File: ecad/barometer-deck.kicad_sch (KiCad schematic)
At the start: 3 parts, among them P1 CF_EXP_LEFT, P2 CF_EXP_RIGHT

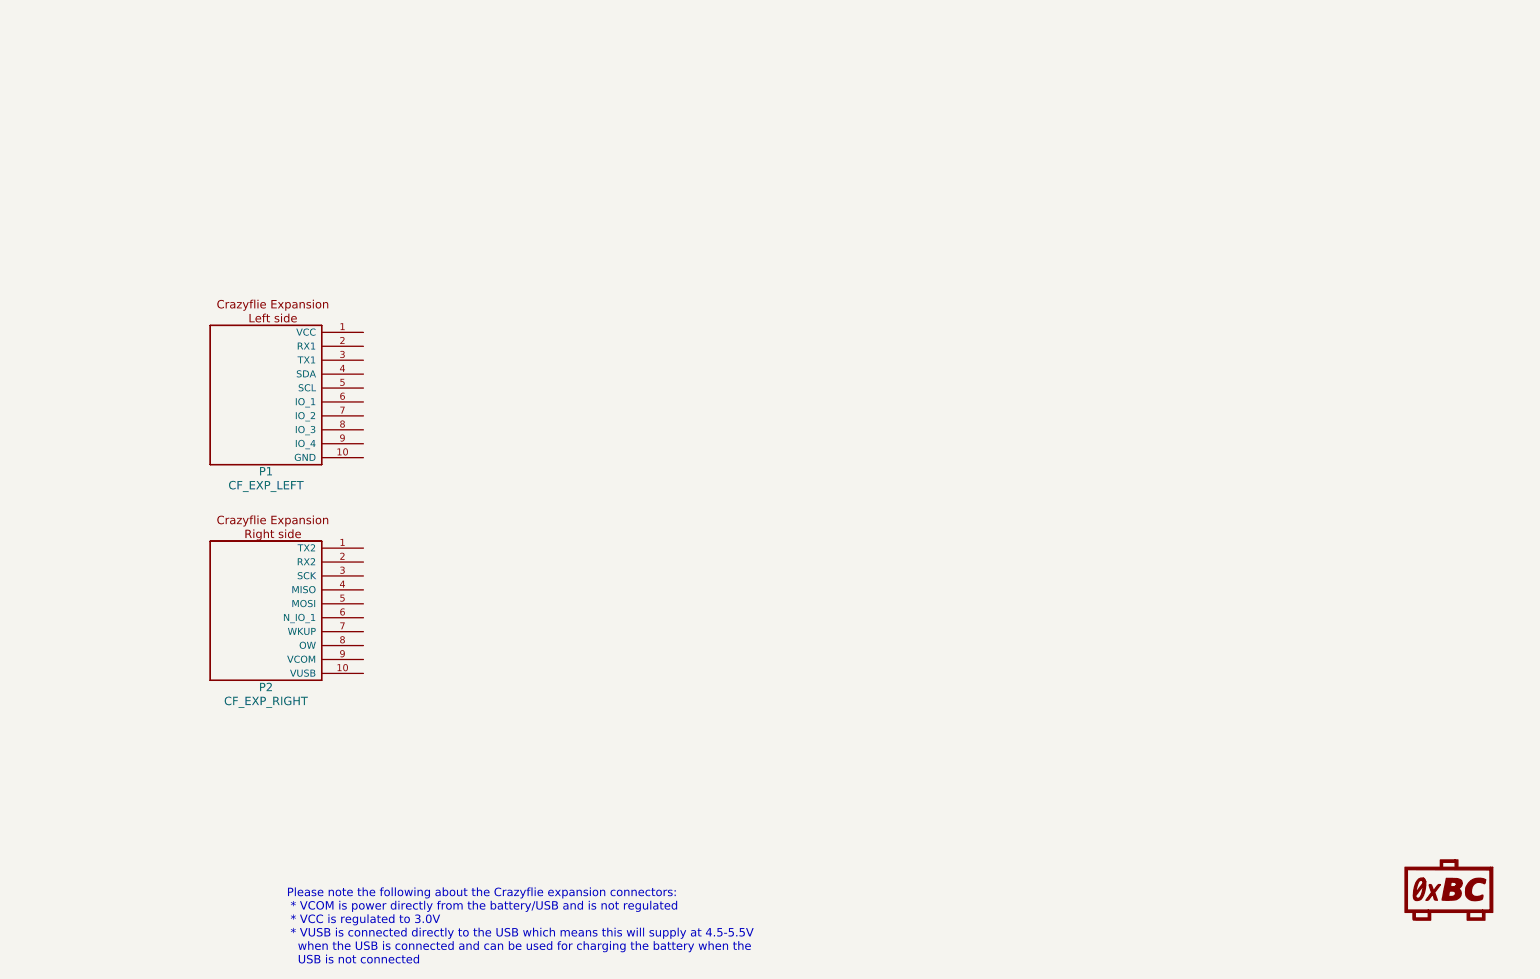
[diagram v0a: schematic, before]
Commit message: Initial schematics, power delviery module
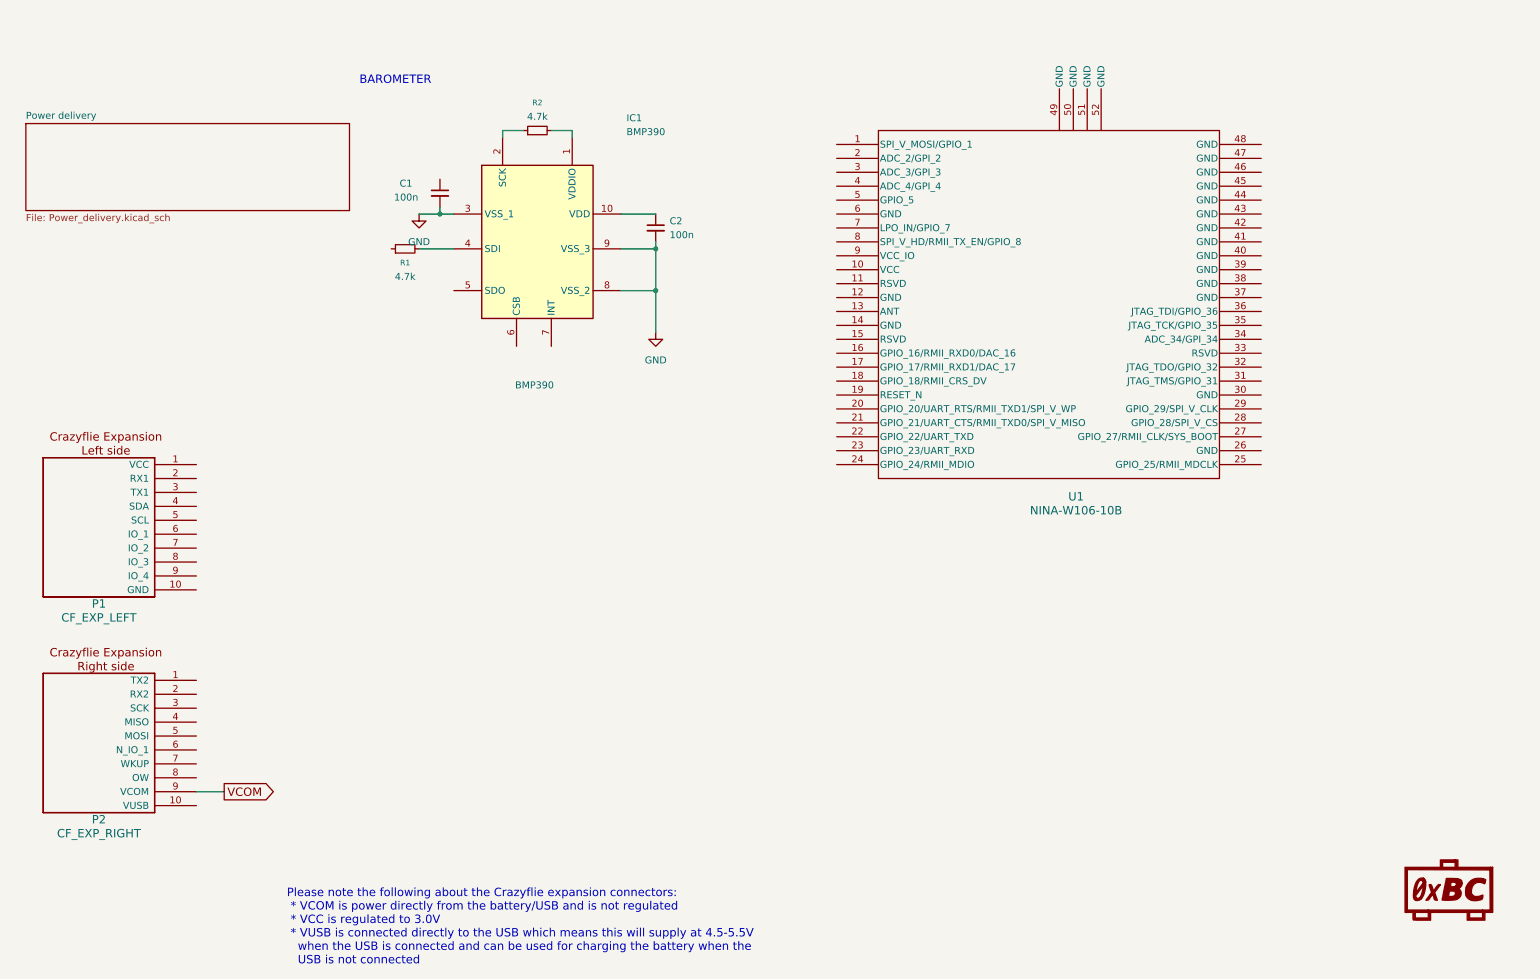
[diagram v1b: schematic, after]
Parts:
- added C1, C2: 100n, symbol PutRocketLab_RCL:C_Small
- added IC1: BMP390, BMP390, symbol BMP390:BMP390
- added R1, R2: 4.7k, symbol Device:R_Small
- added U1: NINA-W106-10B, NINA-W106_UBL, symbol NINA-W106_UBL:NINA-W106-10B
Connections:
- net VCOM: now reaches P2.9 (VCOM)
- new net: IC1.4 (SDI), R1.2
- new net: C2.1, IC1.10 (VDD)
- new net: IC1.2 (SCK), R2.1
- new net: IC1.1 (VDDIO), R2.2
- new net GND: C1.2, C2.2, IC1.3 (VSS_1), IC1.8 (VSS_2), IC1.9 (VSS_3)
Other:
- added sheet Power delivery (Power_delivery.kicad_sch)
- note added: "BAROMETER"
- moved on the sheet: P1, P2

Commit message: updated schematic
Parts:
- added C5, C6: 100n, symbol PutRocketLab_RCL:C_Small
- added D1, D2: LED, symbol Device:LED
- added R3, R4: 1k, symbol Device:R_Small
- added TP1, TP2, TP3, TP4, TP5: TestPoint, symbol Connector:TestPoint
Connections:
- net GND: now also P1.10 (GND), U1.12 (GND), U1.14 (GND), U1.26 (GND), U1.30 (GND), U1.37 (GND), U1.38 (GND), U1.39 (GND), U1.40 (GND), U1.41 (GND), U1.42 (GND), U1.43 (GND), U1.44 (GND), U1.45 (GND), U1.46 (GND), U1.47 (GND), U1.48 (GND), U1.49 (GND), U1.50 (GND), U1.51 (GND), U1.52 (GND), U1.6 (GND), C5.2, C6.2, D1.1 (K), D2.1 (K), TP1.1
- net +3.3V: now reaches R1.1
- net +3.3V: now also C1.1, C2.1, IC1.1 (VDDIO), IC1.10 (VDD), IC1.5 (SDO), IC1.6 (CSB), R2.2, U1.10 (VCC), U1.9 (VCC_IO), C5.1, C6.1, R3.1
- net SDA: now reaches IC1.4 (SDI), R1.2
- net SDA: now also U1.21 (GPIO_21/UART_CTS/RMII_TXD0/SPI_V_MISO)
- net SCK: now reaches IC1.2 (SCK), R2.1
- net SCK: now also U1.24 (GPIO_24/RMII_MDIO)
- net RST: now reaches U1.19 (RESET_N)
- net RST: now also TP2.1
- net TXD: now reaches U1.22 (GPIO_22/UART_TXD)
- net TXD: now also TP5.1
- net RXD: now reaches U1.23 (GPIO_23/UART_RXD)
- net RXD: now also TP4.1
- net BOOT: now reaches U1.27 (GPIO_27/RMII_CLK/SYS_BOOT)
- net BOOT: now also TP3.1
- net WIFI_LED: now reaches U1.5 (GPIO_5)
- net WIFI_LED: now also R4.1
- new net: D2.2 (A), R4.2
- new net: D1.2 (A), R3.2
- no-connect marks 0 -> 1
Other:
- note added: "LED INDICATORS"
- note added: "PROGRAMING"
- moved on the sheet: C1, C2, IC1, R1, R2

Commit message: LDO change
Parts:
- added C7: 100n, symbol PutRocketLab_RCL:C_Small
- added R5: 10k, symbol Device:R_Small
- added TP6: TestPoint, symbol Connector:TestPoint
- added U2: DS2431, Package_TO_SOT_THT:TO-92_Inline, symbol Memory_EEPROM:DS2431
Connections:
- net +3.3V: now also R5.1, TP6.1
- net GND: now also C7.2, U2.1 (GND)
- net RST: now also C7.1, R5.2
- net OW: now reaches P2.8 (OW)
- net OW: now also U2.2 (IO)
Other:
- note added: "DECK DETECTION"

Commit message: Schematic reorder
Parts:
- added C8, C9: 1u, symbol PutRocketLab_RCL:C_Small
- added U3: ~, symbol NCP177AMX330TCG :NCP177AMX330TCG_
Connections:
- net GND: now also C8.2, C9.2, U3. (VOUT)
- net VCOM: now also C8.1, U3. (VOUT)
- new net: C9.1, U3. (VOUT)
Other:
- removed sheet Power delivery
- note added: "Power delivery"
- moved on the sheet: C1, C2, C5, C6, C7, D1, D2, IC1, R1, R2, R3, R4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

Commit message: LDO Change
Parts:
- removed C8, C9: 1u, symbol PutRocketLab_RCL:C_Small
- removed U3: ~, symbol NCP177AMX330TCG :NCP177AMX330TCG_
- added C10: 100n, symbol PutRocketLab_RCL:C_Small
- added C3, C4: 1u, symbol PutRocketLab_RCL:C_Small
- added IC2: MIC5353-3.3YMT-TR, SON50P160X160X60-7N-D, symbol MIC5353-3_3YMT-TR:MIC5353-3.3YMT-TR
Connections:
- net +3.3V: now also C4.1, IC2.4 (VOUT)
- net GND: now also C10.1, C3.1, C4.2, IC2.1 (EN), IC2.2 (GND), IC2.7 (EP)
- net VCOM: now also C3.2, IC2.3 (VIN)
- new net: C10.2, IC2.6 (BYP)

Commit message: footprint assigment
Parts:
- C1: renamed from C3; footprint (none) -> Capacitor_SMD:C_0402_1005Metric
- C2: renamed from C10; footprint (none) -> Capacitor_SMD:C_0402_1005Metric
- C3: renamed from C4; value 1u -> 10u; footprint (none) -> Capacitor_SMD:C_0402_1005Metric
- C4: renamed from C1; footprint (none) -> Capacitor_SMD:C_0402_1005Metric
- C5: renamed from C2; footprint (none) -> Capacitor_SMD:C_0402_1005Metric
- C6: renamed from C7; footprint (none) -> Capacitor_SMD:C_0402_1005Metric
- C7: renamed from C5; footprint (none) -> Capacitor_SMD:C_0402_1005Metric
- C8: renamed from C6; footprint (none) -> Capacitor_SMD:C_0402_1005Metric
- D1, D2: footprint (none) -> LED_SMD:LED_0603_1608Metric
- IC1: renamed from IC2; footprint SON50P160X160X60-7N-D -> MIC5353-3_3YMT-TR:SON50P160X160X60-7N-D
- IC2: renamed from IC1; footprint BMP390 -> BMP390:BMP390
- P1, P2: footprint (none) -> Connector_PinSocket_2.00mm:PinSocket_1x10_P2.00mm_Vertical
- R1, R2: footprint (none) -> Resistor_SMD:R_0402_1005Metric
- R3: renamed from R5; footprint (none) -> Resistor_SMD:R_0402_1005Metric
- R4: renamed from R3; footprint (none) -> Resistor_SMD:R_0402_1005Metric
- R5: renamed from R4; footprint (none) -> Resistor_SMD:R_0402_1005Metric
- TP1: renamed from TP5; footprint (none) -> Connector_PinHeader_2.54mm:PinHeader_1x01_P2.54mm_Vertical
- TP2: renamed from TP4; footprint (none) -> Connector_PinHeader_2.54mm:PinHeader_1x01_P2.54mm_Vertical
- TP3, TP6: footprint (none) -> Connector_PinHeader_2.54mm:PinHeader_1x01_P2.54mm_Vertical
- TP4: renamed from TP2; footprint (none) -> Connector_PinHeader_2.54mm:PinHeader_1x01_P2.54mm_Vertical
- TP5: renamed from TP1; footprint (none) -> Connector_PinHeader_2.54mm:PinHeader_1x01_P2.54mm_Vertical
- U1: footprint NINA-W106_UBL -> NINA-W106_UBL:NINA-W106_UBL
- U2: footprint Package_TO_SOT_THT:TO-92_Inline -> Package_TO_SOT_SMD:SOT-23-3
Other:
- moved on the sheet: C1, C2, C3, IC1

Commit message: jtag support
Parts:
- removed TP1, TP2, TP3, TP4, TP5, TP6: TestPoint, Connector_PinHeader_2.54mm:PinHeader_1x01_P2.54mm_Vertical, symbol Connector:TestPoint
- added J1: JTAG_EDGE, Connector_PinHeader_1.27mm:PinHeader_2x05_P1.27mm_Horizontal, symbol Connector_Generic:Conn_02x05_Odd_Even
- added R6: 330, symbol Device:R_Small
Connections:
- net +3.3V: now also J1.1 (Pin_1)
- net GND: now also J1.3 (Pin_3), J1.5 (Pin_5), J1.9 (Pin_9)
- net NINA_JTAG_TMS: now reaches U1.31 (JTAG_TMS/GPIO_31)
- net NINA_JTAG_TMS: now also J1.2 (Pin_2)
- net NINA_JTAG_TDO: now reaches U1.32 (JTAG_TDO/GPIO_32)
- net NINA_JTAG_TDO: now also J1.6 (Pin_6)
- net NINA_JTAG_TCK: now reaches U1.35 (JTAG_TCK/GPIO_35)
- net NINA_JTAG_TCK: now also J1.4 (Pin_4)
- net NINA_JTAG_TDI: now reaches U1.36 (JTAG_TDI/GPIO_36)
- net NINA_JTAG_TDI: now also J1.8 (Pin_8)
- net RST renamed NINA_NRST
- net NINA_NRST: now also R6.2
- new net: J1.10 (Pin_10), R6.1
- no-connect marks 1 -> 2
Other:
- moved on the sheet: C1, C2, C3, C4, C5, C6, C7, C8, IC1, IC2, R1, R2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

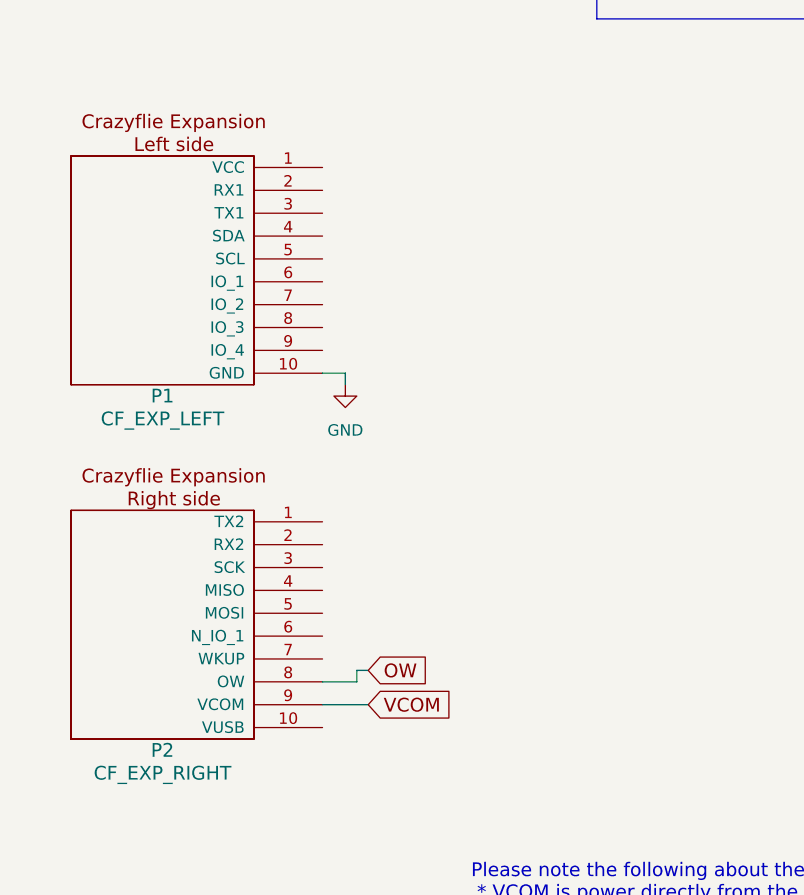
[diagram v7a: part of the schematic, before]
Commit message: schematic update
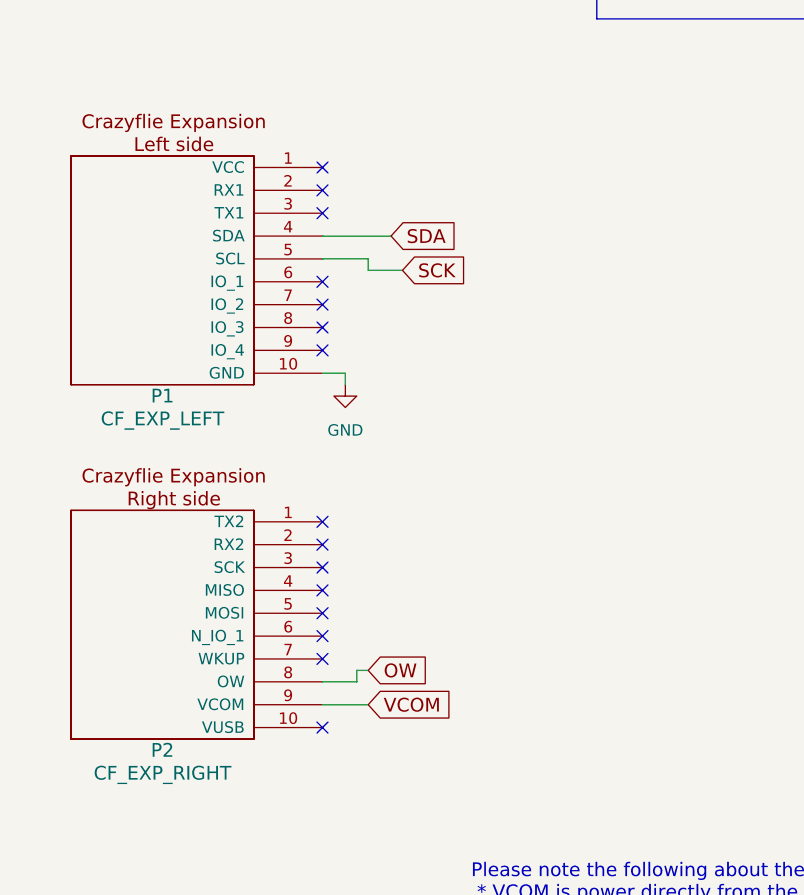
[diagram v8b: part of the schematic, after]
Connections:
- net SCK: now also P1.5 (SCL)
- net SDA: now also P1.4 (SDA)
- no-connect marks 2 -> 17
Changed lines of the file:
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@@
+	)
+	(no_connect
+		(at 44.45 115.57)
+	)
+	(no_connect
+		(at 44.45 134.62)
+	)
+	(no_connect
+		(at 44.45 157.48)
+	)
+	(no_connect
+		(at 44.45 95.25)
+	)
+	(no_connect
+		(at 44.45 107.95)
+	)
+	(no_connect
+		(at 44.45 113.03)
+	)
+	(no_connect
+		(at 44.45 139.7)
 	)
 	(no_connect
@@
 	)
 	(no_connect
+		(at 44.45 97.79)
+	)
+	(no_connect
+		(at 44.45 149.86)
+	)
+	(no_connect
+		(at 44.45 142.24)
+	)
+	(no_connect
+		(at 44.45 110.49)
+	)
+	(no_connect
+		(at 44.45 137.16)
+	)
+	(no_connect
+		(at 44.45 144.78)
+	)
+	(no_connect
+		(at 44.45 100.33)
+	)
+	(no_connect
+		(at 44.45 147.32)
+	)
+	(no_connect
 		(at 149.86 135.89)
 	)
@@
 	(wire
 		(pts
+			(xy 44.45 102.87) (xy 52.07 102.87)
+		)
+		(stroke
+			(width 0)
+			(type default)
+		)
+	)
+	(wire
+		(pts
 			(xy 97.79 58.42) (xy 97.79 49.53)
 		)
@@
 	(wire
 		(pts
+			(xy 53.34 106.68) (xy 49.53 106.68)
+		)
+		(stroke
+			(width 0)
+			(type default)
+		)
+	)
+	(wire
+		(pts
 			(xy 217.17 25.4) (xy 219.71 25.4)
 		)
@@
 	(wire
 		(pts
+			(xy 49.53 106.68) (xy 49.53 105.41)
+		)
+		(stroke
+			(width 0)
+			(type default)
+		)
+	)
+	(wire
+		(pts
 			(xy 222.25 144.78) (xy 222.25 151.13)
 		)
@@
 		(pts
 			(xy 256.54 81.28) (xy 264.16 81.28)
+		)
+		(stroke
+			(width 0)
+			(type default)
+		)
+	)
+	(wire
+		(pts
+			(xy 49.53 105.41) (xy 44.45 105.41)
 		)
 		(stroke
@@
 		)
 	)
+	(global_label "SCK"
+		(shape input)
+		(at 53.34 106.68 0)
+		(fields_autoplaced yes)
+		(effects
+			(font
+				(size 1.524 1.524)
+			)
+			(justify left)
+		)
+		(property "Intersheetrefs" "${INTERSHEET_REFS}"
+			(at 60.6362 106.68 0)
+			(effects
+				(font
+					(size 1.27 1.27)
+				)
+				(justify left)
+				(hide yes)
+			)
+		)
+	)
 	(global_label "NINA_NRST"
 		(shape input)
@@
 			(effects
 				(font
+					(size 1.27 1.27)
+				)
+				(justify left)
+				(hide yes)
+			)
+		)
+	)
+	(global_label "SDA"
+		(shape input)
+		(at 52.07 102.87 0)
+		(fields_autoplaced yes)
+		(effects
+			(font
+				(size 1.524 1.524)
+			)
+			(justify left)
+		)
+		(property "Intersheetrefs" "${INTERSHEET_REFS}"
+			(at 59.1485 102.87 0)
+			(effects
+				(font
